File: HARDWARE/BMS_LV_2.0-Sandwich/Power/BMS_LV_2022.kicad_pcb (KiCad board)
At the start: 4 copper layers, 90 x 45 mm, 119 parts, among them J1 Conn_01x26, J11 Conn_01x07_Female, J2 AS214-97PN, J4 Battery+, J5 Battery-, J6 Conn_01x09_Female, Q1 BC846, Q10 BSS138, Q12 SIR5607DP-T1-RE3, Q13 SIR5607DP-T1-RE3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

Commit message: Zmieniono polozenie bezpiecznikow, dodano ledy sygnalizujące czy bezpiecznik jest cały
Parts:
- added D18: LED_RED, LED_SMD:LED_0603_1608Metric, F.Cu at (121.7, 122.8)
- added D19: LED_RED, LED_SMD:LED_0603_1608Metric, F.Cu at (124.6, 122.9)
- added R70: 330, Resistor_SMD:R_0603_1608Metric, F.Cu at (121.7, 119.8)
- added R71: 330, Resistor_SMD:R_0603_1608Metric, F.Cu at (124.6, 119.9)
- moved F4 33.8 mm to (144.2, 95.3), turned to -90 degrees
- moved F3 29.5 mm to (140.7, 95.3), turned to -90 degrees
- moved H1 9.12 mm to (141.5, 83.8)
- moved R65 7.86 mm to (142.8, 89.1)
- moved R66 7.86 mm to (142.8, 87.6)
- moved C13 5.54 mm to (142.0, 105.8), turned to -90 degrees
- moved C18 5.48 mm to (148.0, 92.8), turned to 180 degrees
- moved R13 4.12 mm to (139.7, 107.8)
- moved R14 4.12 mm to (139.7, 106.3)
- turned J2 to 0 degrees
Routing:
- net /V_Out_Pin_2: track 8.65 -> 28.7 mm, vias 7 -> 30
- net /VoltageFuseMeasure: track 24.0 -> 14.3 mm, vias 3 -> 2
- net /V_Out_Pin_1: track 13.0 -> 22.3 mm, vias 10 -> 8
- net Net-(J2-PadH): track 23.2 -> 31.9 mm
- net VCC: track 39.4 -> 45.9 mm
- net Net-(Q1-C): track 3.08 -> 9.51 mm
- net /VCC_Pin: track 17.6 -> 11.8 mm
- net /CS_IP+: track 9.36 -> 3.56 mm, vias 12 -> 11
- net GND: track 23.6 -> 19.7 mm, vias 171 -> 194
- net +5V: track 35.6 -> 33.5 mm
- net /eFuse/Gate: track 50.0 -> 48.1 mm
- net Net-(D18-A): track 0.00 -> 1.39 mm
- net Net-(D19-A): track 0.00 -> 1.39 mm
- net Net-(F3-Pad1): vias 13 -> 8
- added copper zone on B.Cu, net /V_Out_Pin_1
- added copper zone on F.Cu, net /V_Out_Pin_1
- added copper zone on In1.Cu, net /V_Out_Pin_1
- added copper zone on In2.Cu, net /V_Out_Pin_1
- added copper zone on B.Cu, net /V_Out_Pin_2
- added copper zone on F.Cu, net /V_Out_Pin_2
- added copper zone on In1.Cu, net /V_Out_Pin_2
- added copper zone on In2.Cu, net /V_Out_Pin_2
- added copper zone on In1.Cu, net Net-(F3-Pad1)
- added copper zone on In2.Cu, net Net-(F3-Pad1)
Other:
- board text added: "FUSE 1 OK"
- board text added: "FUSE 2 OK"

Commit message: sync
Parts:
- R70, R71: value 330 -> 1k5
- moved R14 16.0 mm to (127.7, 116.9), turned to 0 degrees
- moved R13 14.2 mm to (127.7, 115.4), turned to 180 degrees
- moved R19 0.68 mm to (144.7, 100.7)
- moved J2 0.36 mm to (125.3, 105.8)
- moved Q15 0.24 mm to (116.5, 85.1)
- moved Q13 0.23 mm to (123.1, 85.1)
- moved Q1 0.21 mm to (147.6, 99.9)
- moved F3 0.20 mm to (140.5, 95.3)
- moved F4 0.20 mm to (144.0, 95.3)
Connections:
- net /USB-DM renamed /USB1-
- net /USB-DP renamed /USB1+
- net Net-(J2-PadJ) renamed /USB-
- net Net-(J2-PadK) renamed /USB+
- C19 pad 2: GNDPWR -> GND
- C20 pad 2: GNDPWR -> GND
- C21 pad 2: GNDPWR -> GND
- C22 pad 2: GNDPWR -> GND
- C23 pad 2: GNDPWR -> GND
- C24 pad 2: GNDPWR -> GND
- J1 pad 16: /CAN+ -> /CAN-
- J1 pad 17: /CAN- -> /CAN+
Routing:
- net /CAN-: track 0.00 -> 58.2 mm, vias 0 -> 1
- net /CAN+: track 0.00 -> 58.2 mm, vias 0 -> 1
- net /USB1-: track 0.00 -> 50.9 mm, vias 0 -> 2
- net /USB1+: track 0.00 -> 50.8 mm, vias 0 -> 2
- net GND: track 19.7 -> 49.3 mm, vias 194 -> 188
- net /Interlock: track 1.57 -> 27.8 mm, vias 1 -> 2
- net GNDPWR: track 24.0 -> 0.00 mm, vias 2 -> 0
- net Net-(LTC68101-C6): track 6.16 -> 22.6 mm, vias 1 -> 2
- net /USB+: track 0.00 -> 11.3 mm
- net /USB-: track 0.00 -> 11.0 mm
- net +3V3: track 86.6 -> 97.2 mm
- net /LTC6810/Balance2/Sx: track 3.87 -> 12.0 mm
- net /CS_IP+: track 3.56 -> 11.0 mm, vias 11 -> 14
- net VCC: track 45.9 -> 49.4 mm
- net Net-(D8-K): track 63.0 -> 66.3 mm
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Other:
- outline, holes or cut-outs redrawn

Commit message: Wersja obu plytek gotowa do sprawdzenia
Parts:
- moved H4 69.7 mm to (196.2, 85.8)
- moved C15 15.5 mm to (139.5, 107.4), turned to 0 degrees
- moved C17 12.0 mm to (139.5, 105.9), turned to 0 degrees
- moved C16 12.0 mm to (139.5, 104.4), turned to 0 degrees
- moved C18 9.23 mm to (143.2, 100.7), turned to 90 degrees
- moved D17 6.75 mm to (188.2, 81.8), turned to -90 degrees
- moved F3 5.67 mm to (146.1, 96.2), turned to 180 degrees
- moved R58 5.23 mm to (190.0, 81.8), turned to -90 degrees
- moved Q7 4.88 mm to (192.8, 81.8), turned to 0 degrees
- moved F4 3.19 mm to (146.1, 92.9), turned to 180 degrees
- moved F1 2.60 mm to (114.1, 98.3)
- moved D18 1.95 mm to (119.8, 122.8)
- moved D19 1.95 mm to (122.6, 122.9)
- moved R70 1.95 mm to (119.8, 119.8)
- moved R71 1.95 mm to (122.6, 119.9)
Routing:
- net /V_Out_Pin_1: track 22.3 -> 47.0 mm
- net /LTC6810/Balance6/Sx: track 59.4 -> 34.8 mm
- net /V_Out_Pin_2: track 28.7 -> 50.4 mm
- net Net-(F3-Pad1): track 0.00 -> 20.8 mm, vias 8 -> 4
- net Net-(LTC68101-Vref1): track 7.58 -> 24.9 mm, vias 0 -> 2
- net Net-(LTC68101-Vreg): track 5.81 -> 20.2 mm
- net Net-(LTC68101-Vref2): track 6.70 -> 18.0 mm, vias 0 -> 2
- net Net-(Q1-C): track 9.51 -> 3.21 mm
- net Net-(D14-K): track 57.6 -> 61.7 mm
- net Net-(D16-K): track 71.6 -> 75.5 mm, vias 63 -> 62
- net /VCC_Pin: track 12.2 -> 14.8 mm
- net +3V3: track 97.2 -> 99.7 mm
- net /USB1+: track 50.8 -> 49.6 mm
- net GND: track 49.3 -> 50.2 mm, vias 188 -> 179
- removed copper zone on B.Cu, net /V_Out_Pin_1
- removed copper zone on F.Cu, net /V_Out_Pin_1
- removed copper zone on In1.Cu, net /V_Out_Pin_1
- removed copper zone on In2.Cu, net /V_Out_Pin_1
- removed copper zone on B.Cu, net /V_Out_Pin_2
- removed copper zone on F.Cu, net /V_Out_Pin_2
- removed copper zone on In1.Cu, net /V_Out_Pin_2
- removed copper zone on In2.Cu, net /V_Out_Pin_2
- removed copper zone on B.Cu, net Net-(F3-Pad1)
- removed copper zone on F.Cu, net Net-(F3-Pad1)
- removed copper zone on In1.Cu, net Net-(F3-Pad1)
- removed copper zone on In2.Cu, net Net-(F3-Pad1)

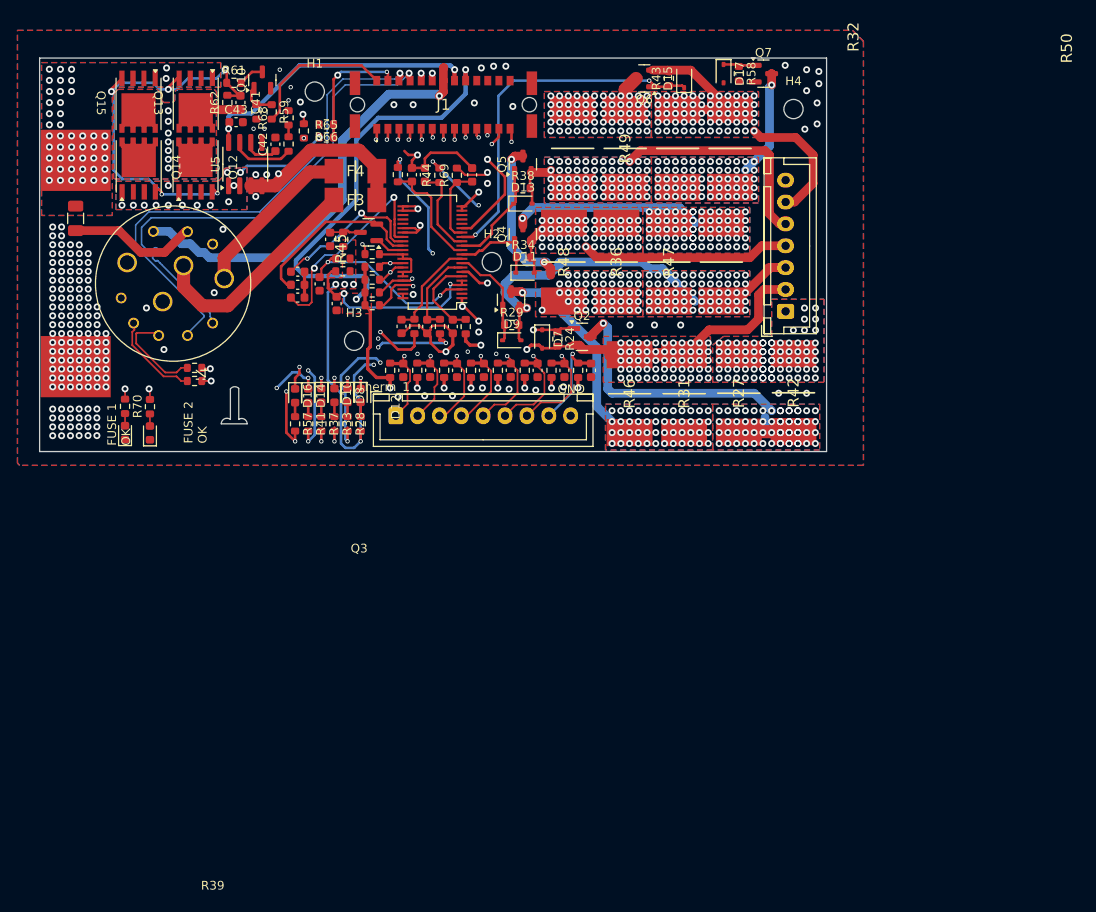
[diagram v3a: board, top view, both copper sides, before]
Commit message: Zmiany w power: nowe bezpieczniki, nowy wymienialny layout dla tych bezpiecznikow, dodano diode zenera dla stabilizacji napięcia, zmiany dla control:  wyjebany eeprom, przesunięty can, zmieniony layout przetwornic, dodano programator i tvs, jeszcze do dokonczenia routing w control.
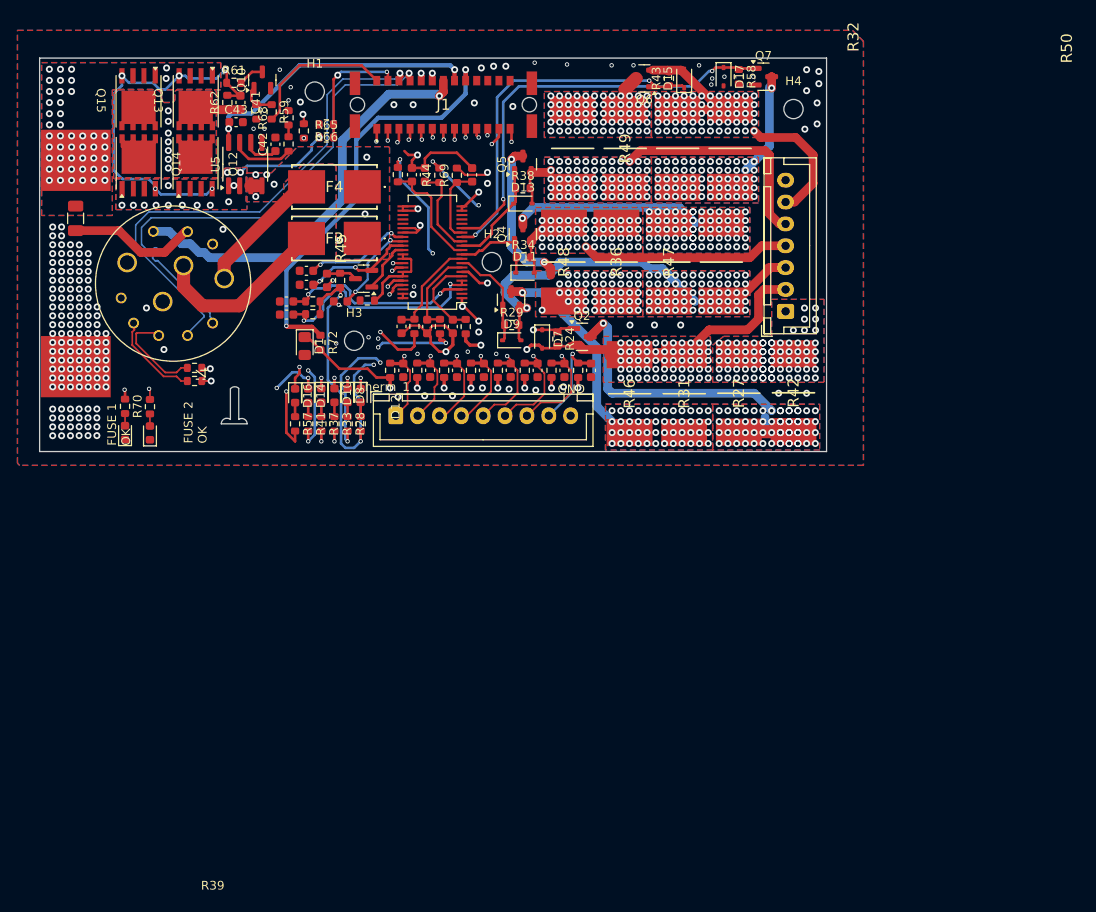
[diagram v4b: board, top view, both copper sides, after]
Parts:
- removed R16, R17, R18, R20: 2.2k, Resistor_SMD:R_0603_1608Metric
- added D1: D_Zener_Small, Diode_SMD:D_0805_2012Metric_Pad1.15x1.40mm_HandSolder, F.Cu at (140.3, 112.9)
- added R72: 100, Resistor_SMD:R_0603_1608Metric, F.Cu at (142.1, 112.5)
- F3, F4: footprint footprints:FUSC6125X279N -> footprints:01550900DR
- moved R10 5.99 mm to (141.2, 107.8)
- moved R11 5.99 mm to (141.2, 109.3)
- moved C16 5.96 mm to (144.4, 107.8), turned to 180 degrees
- moved C14 5.86 mm to (138.2, 109.3), turned to 180 degrees
- moved Q1 5.33 mm to (147.1, 105.2)
- moved R12 5.33 mm to (147.5, 107.7)
- moved F3 5.02 mm to (143.7, 100.6)
- moved C18 4.71 mm to (142.9, 105.4)
- moved R19 4.71 mm to (144.4, 105.4)
- moved C13 4.28 mm to (138.2, 107.8), turned to 180 degrees
- moved C15 3.22 mm to (140.5, 104.3), turned to 180 degrees
- moved F4 3.00 mm to (143.7, 94.7)
- moved C17 1.00 mm to (140.5, 105.9), turned to 180 degrees
- moved Q12 0.36 mm to (132.6, 92.1)
- moved Q14 0.36 mm to (126.1, 92.1)
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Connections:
- R51 pad 1: +3V3 -> /Thermistors/3V3_zener
- R52 pad 1: +3V3 -> /Thermistors/3V3_zener
- R53 pad 1: +3V3 -> /Thermistors/3V3_zener
- R54 pad 1: +3V3 -> /Thermistors/3V3_zener
- R55 pad 1: +3V3 -> /Thermistors/3V3_zener
- R56 pad 1: +3V3 -> /Thermistors/3V3_zener
- R63 pad 1: +3V3 -> /Thermistors/3V3_zener
- R64 pad 1: +3V3 -> /Thermistors/3V3_zener
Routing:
- net +3V3: track 99.7 -> 47.6 mm, vias 10 -> 2
- net /Thermistors/3V3_zener: track 0.00 -> 48.4 mm, vias 0 -> 8
- net Net-(F3-Pad1): track 20.8 -> 0.69 mm, vias 4 -> 7
- net /LTC6810/Balance6/Sx: track 34.8 -> 47.8 mm
- net Net-(LTC68101-Vref1): track 24.9 -> 12.2 mm
- net /MOSI: track 30.8 -> 22.0 mm
- net Net-(LTC68101-Vref2): track 18.0 -> 10.4 mm
- net Net-(LTC68101-Vreg): track 20.2 -> 12.8 mm, vias 0 -> 2
- net /MISO: track 27.5 -> 20.5 mm
- net /V_Out_Pin_2: track 50.4 -> 43.6 mm, vias 2 -> 1
- net /V_Out_Pin_1: track 47.0 -> 41.5 mm
- net /eFuse/Gate: track 48.1 -> 43.6 mm
- net +BATT: track 76.2 -> 80.2 mm, vias 82 -> 80
- net Net-(LTC68101-C6): track 22.6 -> 26.3 mm
- net GND: track 50.2 -> 46.8 mm, vias 179 -> 192
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- added copper zone on B.Cu, net Net-(F3-Pad1)
- added copper zone on F.Cu, net Net-(F3-Pad1)
- added copper zone on In1.Cu, net Net-(F3-Pad1)
- added copper zone on In2.Cu, net Net-(F3-Pad1)
- removed copper zone on F.Cu, net +3V3

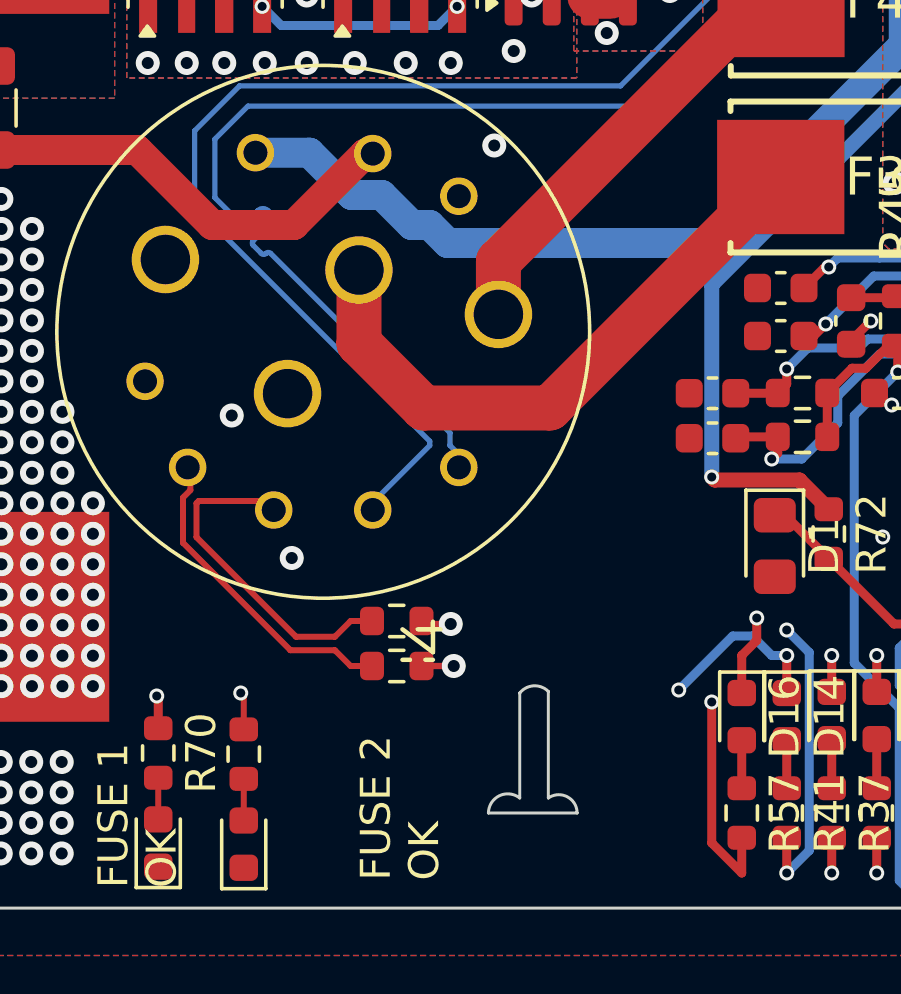
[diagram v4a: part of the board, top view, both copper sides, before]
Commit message: Pierwsza wersja bez błędów DRC/ERC, skończony routing plytki control
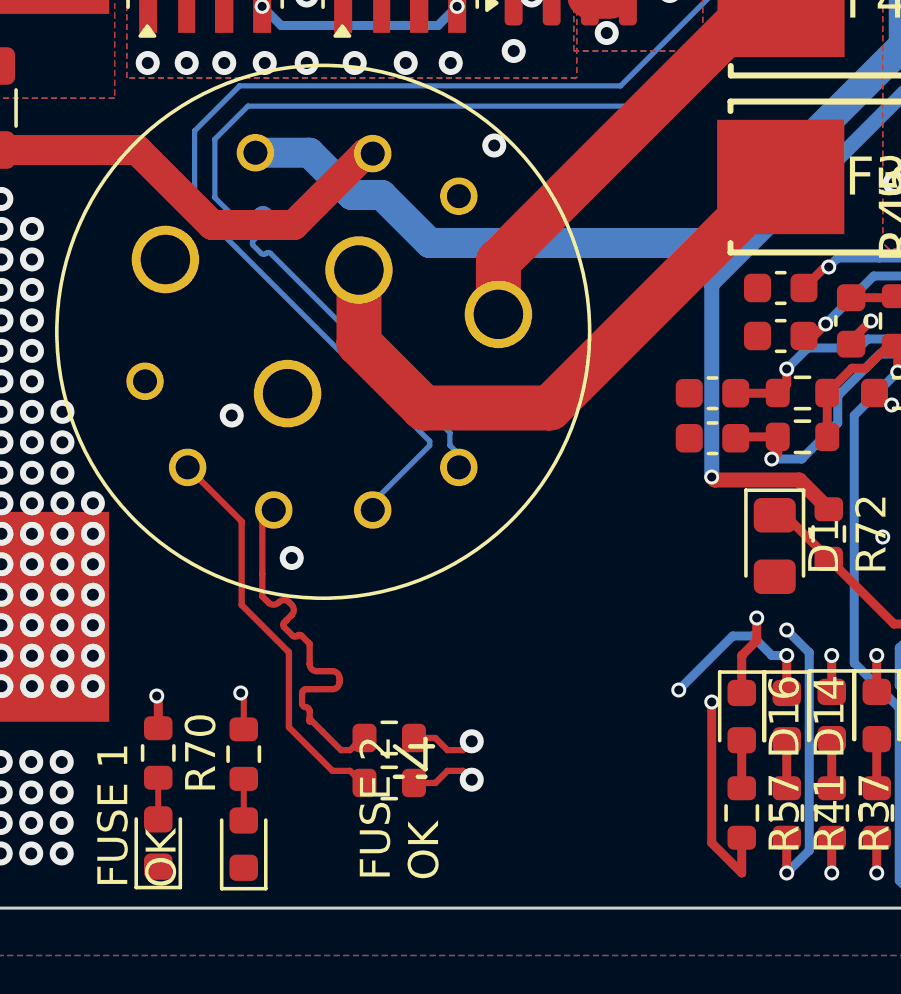
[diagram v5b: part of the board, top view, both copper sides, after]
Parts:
- moved R13 3.91 mm to (127.5, 119.3)
- moved R14 3.91 mm to (127.5, 120.8)
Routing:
- net /USB1+: track 50.3 -> 53.9 mm
- net /USB1-: track 50.3 -> 53.9 mm
- net /USB-: track 11.0 -> 13.4 mm
- net /USB+: track 11.2 -> 13.3 mm
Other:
- outline, holes or cut-outs redrawn
